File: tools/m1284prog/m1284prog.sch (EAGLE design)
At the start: 10 parts, among them IC1 ATMEGA644-20PU, J1 AVR_SPI_PROG_3X2PTH

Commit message: Update several tool boards.
+ AEPRO had the wrong socket size; the ZIF footprint was for
  a narrow 28-pin DIP.
+ AEPRO was missing an inverter on the LEDs.
+ M328PGM had a serial line tied to RST: any attempt at using the
  UART caused the board to reset.
+ M1284PGM had no silkscreen markings to identify the board.
+ M1284PGM had no decoupling capacitor for the MCU.
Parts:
- added C1: 0.1uF, capacitor-wima:C2,5-3
- R1: value (none) -> 10K
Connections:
- net GND: now also C1.2
- net VCC: now also C1.1
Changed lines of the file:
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@@
 <drawing>
 <settings>
-<setting alwaysvectorfont="yes"/>
+<setting alwaysvectorfont="no"/>
 <setting verticaltext="up"/>
 </settings>
@@
 <part name="SUPPLY1" library="SparkFun-PowerSymbols" deviceset="VCC" device=""/>
 <part name="GND1" library="SparkFun-PowerSymbols" deviceset="GND" device=""/>
-<part name="R1" library="SparkFun-Resistors" deviceset="RESISTOR" device="AXIAL-0.3" value=" "/>
+<part name="R1" library="SparkFun-Resistors" deviceset="RESISTOR" device="AXIAL-0.3" value="10K"/>
 <part name="S1" library="SparkFun-Retired" deviceset="TAC_SWITCH" device="PTH"/>
 <part name="J1" library="SparkFun-Connectors" deviceset="AVR_SPI_PROG_3X2" device="PTH"/>
@@
 <part name="GND5" library="SparkFun-PowerSymbols" deviceset="GND" device=""/>
 <part name="CN1" library="microbuilder" deviceset="FTDIUSBCABLE" device=""/>
+<part name="C1" library="capacitor-wima" library_urn="urn:adsk.eagle:library:116" deviceset="C" device="2,5-3" package3d_urn="urn:adsk.eagle:package:5436/1" value="0.1uF"/>
 </parts>
 <sheets>
@@
 <attribute name="VALUE" x="0" y="-2.54" size="1.27" layer="96" rot="R180"/>
 </instance>
+<instance part="C1" gate="G$1" x="-27.94" y="25.4" smashed="yes">
+<attribute name="NAME" x="-26.416" y="25.781" size="1.778" layer="95"/>
+<attribute name="VALUE" x="-26.416" y="20.701" size="1.778" layer="96"/>
+</instance>
 </instances>
 <busses>
@@
 <wire x1="-5.08" y1="20.32" x2="-22.86" y2="20.32" width="0.1524" layer="91"/>
 <pinref part="GND1" gate="1" pin="GND"/>
-<wire x1="-22.86" y1="20.32" x2="-22.86" y2="7.62" width="0.1524" layer="91"/>
+<wire x1="-22.86" y1="20.32" x2="-22.86" y2="17.78" width="0.1524" layer="91"/>
 <pinref part="S1" gate="S" pin="2"/>
+<wire x1="-22.86" y1="17.78" x2="-22.86" y2="7.62" width="0.1524" layer="91"/>
 <wire x1="-22.86" y1="7.62" x2="-22.86" y2="2.54" width="0.1524" layer="91"/>
 <wire x1="-33.02" y1="27.94" x2="-33.02" y2="7.62" width="0.1524" layer="91"/>
@@
 <wire x1="10.16" y1="22.86" x2="10.16" y2="7.62" width="0.1524" layer="91"/>
 <wire x1="10.16" y1="7.62" x2="-22.86" y2="7.62" width="0.1524" layer="91"/>
+<pinref part="C1" gate="G$1" pin="2"/>
+<wire x1="-27.94" y1="20.32" x2="-27.94" y2="17.78" width="0.1524" layer="91"/>
+<wire x1="-27.94" y1="17.78" x2="-22.86" y2="17.78" width="0.1524" layer="91"/>
+<junction x="-22.86" y="17.78"/>
 </segment>
 <segment>
@@
 <wire x1="25.4" y1="25.4" x2="-22.86" y2="25.4" width="0.1524" layer="91"/>
 <pinref part="SUPPLY1" gate="G$1" pin="VCC"/>
-<wire x1="-22.86" y1="25.4" x2="-22.86" y2="50.8" width="0.1524" layer="91"/>
+<wire x1="-22.86" y1="25.4" x2="-22.86" y2="30.48" width="0.1524" layer="91"/>
 <pinref part="R1" gate="G$1" pin="2"/>
+<wire x1="-22.86" y1="30.48" x2="-22.86" y2="50.8" width="0.1524" layer="91"/>
 <wire x1="-22.86" y1="50.8" x2="-22.86" y2="58.42" width="0.1524" layer="91"/>
 <wire x1="-33.02" y1="50.8" x2="-22.86" y2="50.8" width="0.1524" layer="91"/>
 <junction x="-22.86" y="50.8"/>
-</segment>
-<segment>
+<pinref part="C1" gate="G$1" pin="1"/>
+<wire x1="-27.94" y1="27.94" x2="-27.94" y2="30.48" width="0.1524" layer="91"/>
+<wire x1="-27.94" y1="30.48" x2="-22.86" y2="30.48" width="0.1524" layer="91"/>
+<junction x="-22.86" y="30.48"/>
+</segment>
+<segment>

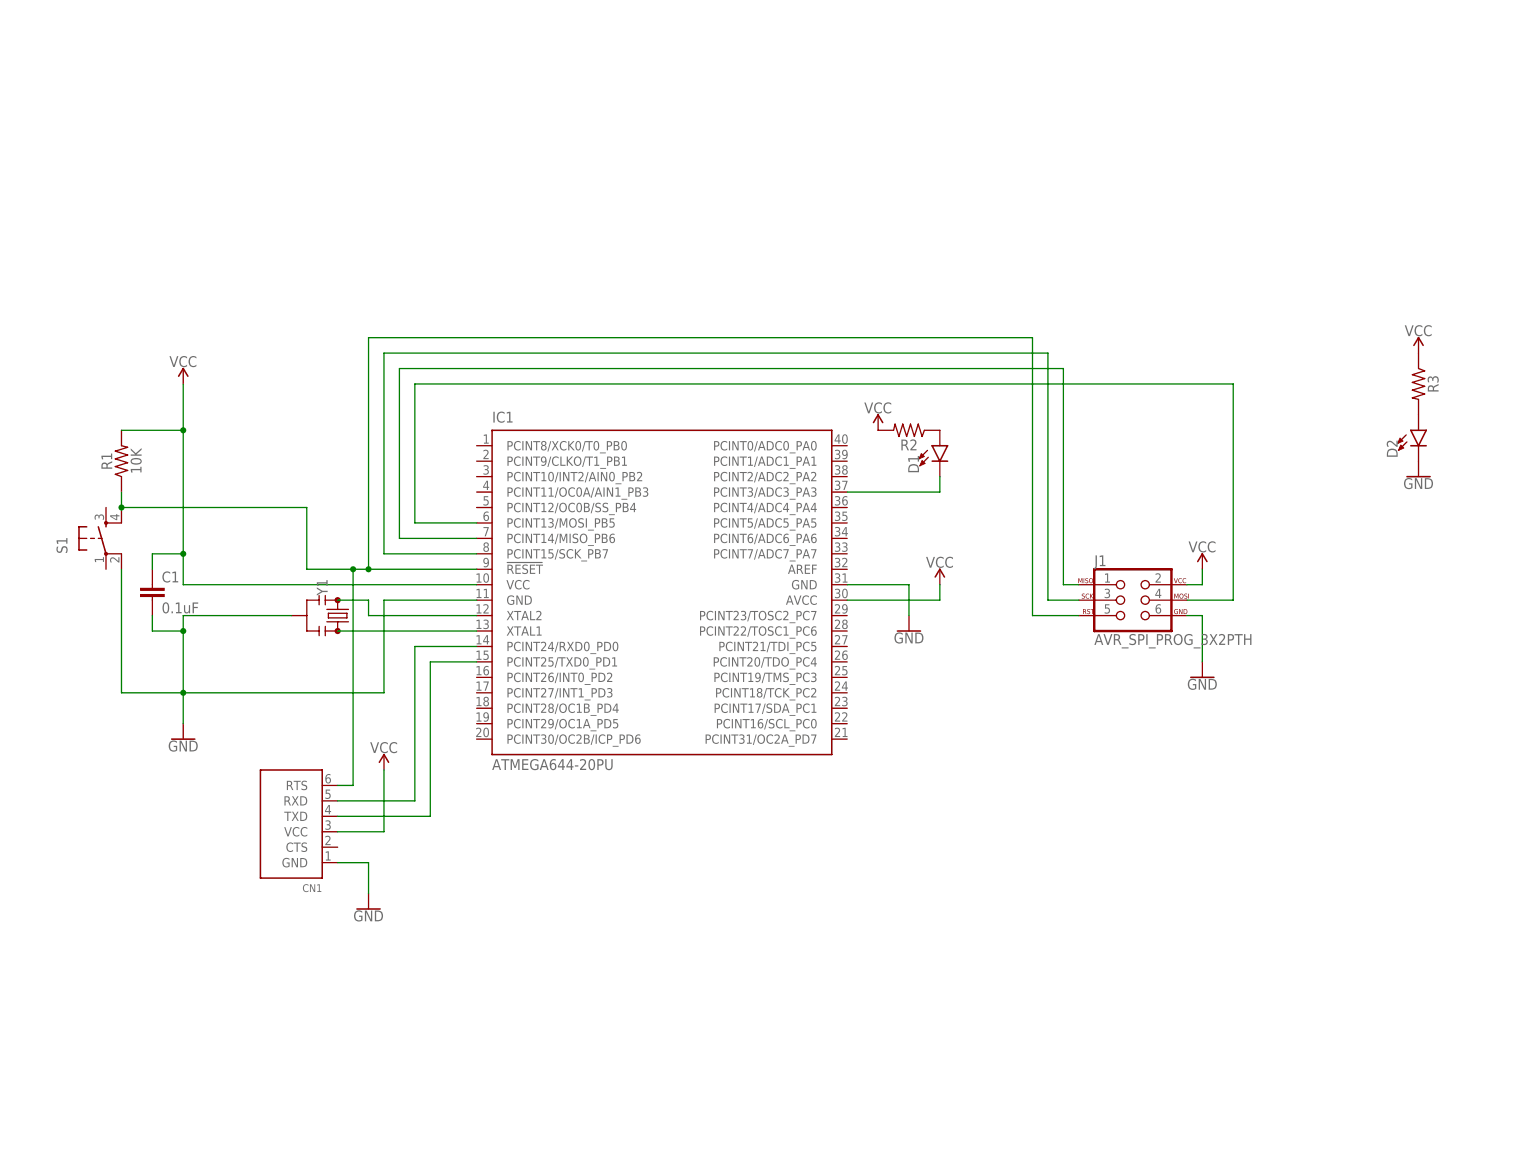
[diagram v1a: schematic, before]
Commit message: Fix UART issues in programmers.
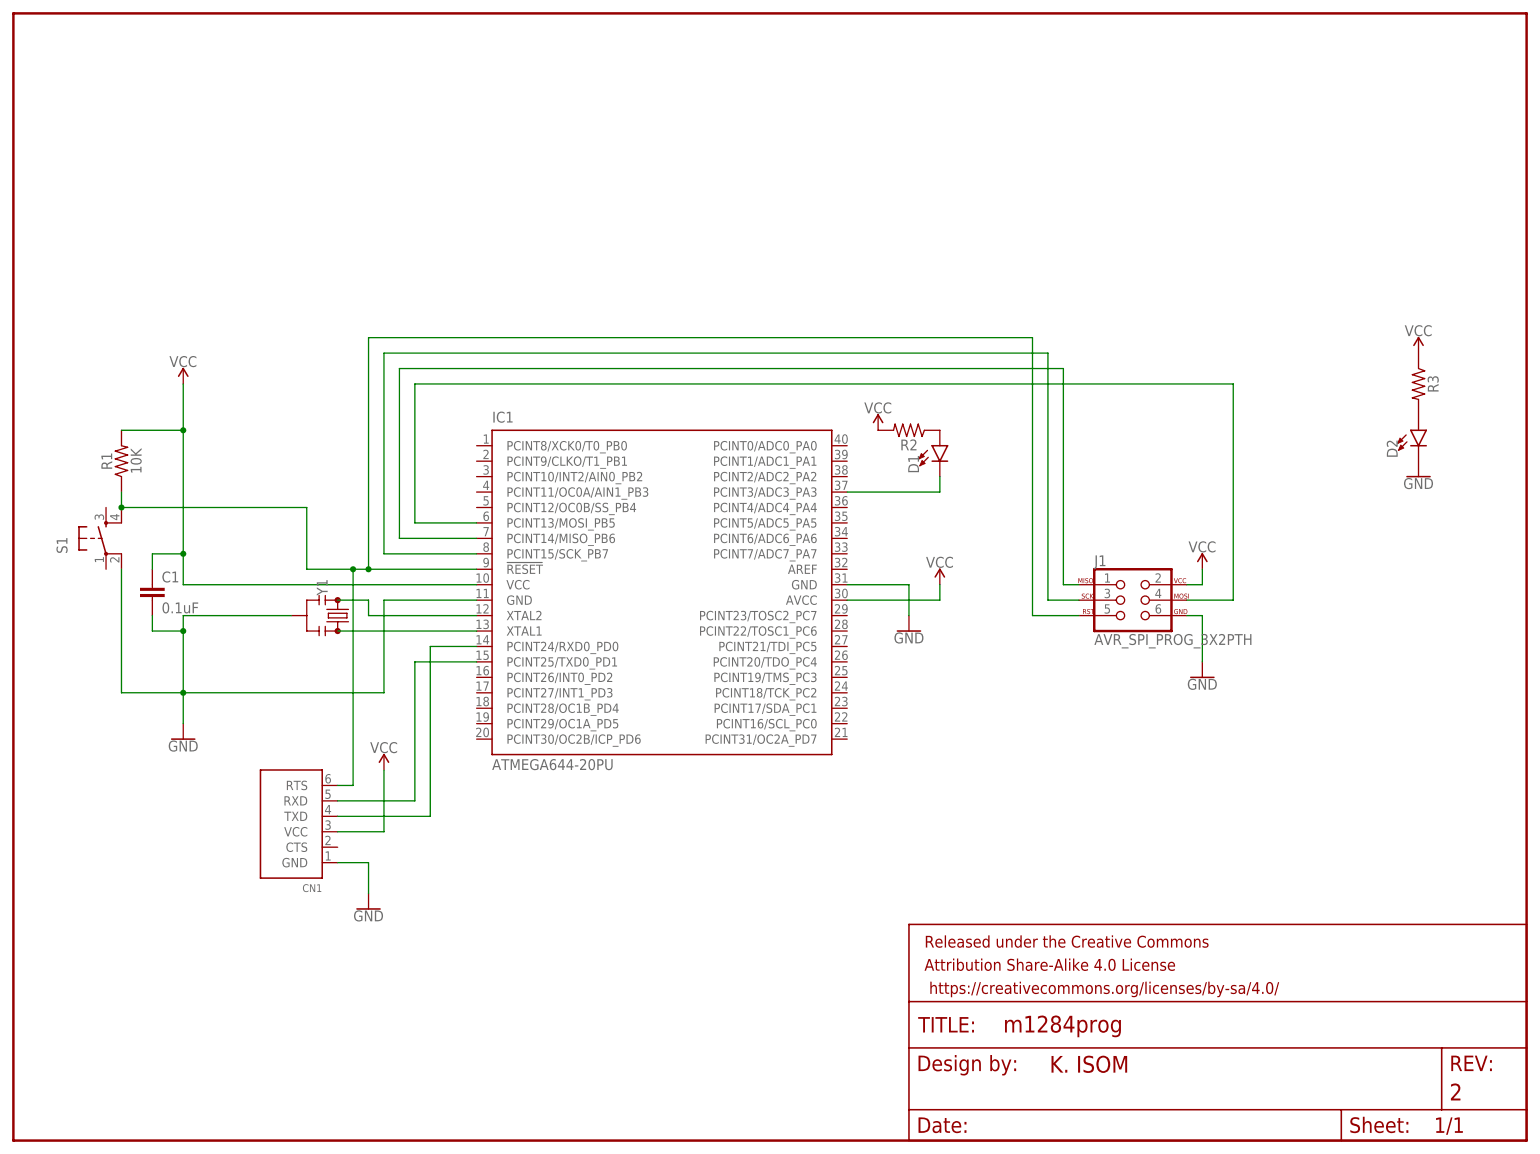
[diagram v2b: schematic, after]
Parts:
- added FRAME1: FRAME-LETTER, SparkFun-Aesthetics:FRAME-LETTER
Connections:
- removed net N$12: CN1.RXD, IC1.PCINT24/RXD0_PD0
- removed net N$13: CN1.TXD, IC1.PCINT25/TXD0_PD1
- new net N$10: CN1.RXD, IC1.PCINT25/TXD0_PD1
- new net N$9: CN1.TXD, IC1.PCINT24/RXD0_PD0
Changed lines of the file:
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@@
 <drawing>
 <settings>
-<setting alwaysvectorfont="no"/>
+<setting alwaysvectorfont="yes"/>
 <setting verticaltext="up"/>
 </settings>
@@
 <layer number="115" name="ReferenceISLANDS" color="7" fill="1" visible="yes" active="yes"/>
 <layer number="116" name="Patch_BOT" color="9" fill="4" visible="yes" active="yes"/>
+<layer number="117" name="PM_Ref" color="26" fill="1" visible="yes" active="yes"/>
 <layer number="118" name="Rect_Pads" color="7" fill="1" visible="yes" active="yes"/>
+<layer number="119" name="PF_Ref" color="31" fill="1" visible="yes" active="yes"/>
+<layer number="120" name="WFL_Ref" color="25" fill="1" visible="yes" active="yes"/>
 <layer number="121" name="_tsilk" color="7" fill="1" visible="yes" active="yes"/>
 <layer number="122" name="_bsilk" color="7" fill="1" visible="yes" active="yes"/>
@@
 <part name="CN1" library="microbuilder" deviceset="FTDIUSBCABLE" device=""/>
 <part name="C1" library="capacitor-wima" library_urn="urn:adsk.eagle:library:116" deviceset="C" device="2,5-3" package3d_urn="urn:adsk.eagle:package:5436/1" value="0.1uF"/>
+<part name="FRAME1" library="SparkFun-Aesthetics" deviceset="FRAME-LETTER" device="">
+<attribute name="DESIGNER" value="K. ISOM"/>
+<attribute name="REV" value="2"/>
+</part>
 </parts>
 <sheets>
@@
 <attribute name="NAME" x="-26.416" y="25.781" size="1.778" layer="95"/>
 <attribute name="VALUE" x="-26.416" y="20.701" size="1.778" layer="96"/>
+</instance>
+<instance part="FRAME1" gate="G$1" x="-50.8" y="-66.04" smashed="yes"/>
+<instance part="FRAME1" gate="V" x="96.52" y="-66.04" smashed="yes">
+<attribute name="LAST_DATE_TIME" x="109.22" y="-64.77" size="2.54" layer="94" font="vector"/>
+<attribute name="SHEET" x="182.88" y="-64.77" size="2.54" layer="94" font="vector"/>
+<attribute name="DRAWING_NAME" x="112.014" y="-48.26" size="2.7432" layer="94" font="vector"/>
+<attribute name="DESIGNER" x="119.634" y="-54.864" size="2.7432" layer="94" font="vector"/>
+<attribute name="REV" x="185.42" y="-59.436" size="2.7432" layer="94" font="vector"/>
 </instance>
 </instances>
@@
 </segment>
 </net>
-<net name="N$12" class="0">
+<net name="N$9" class="0">
+<segment>
+<pinref part="CN1" gate="G$1" pin="TXD"/>
+<wire x1="2.54" y1="-12.7" x2="17.78" y2="-12.7" width="0.1524" layer="91"/>
+<pinref part="IC1" gate="G$1" pin="PCINT24/RXD0_PD0"/>
+<wire x1="17.78" y1="15.24" x2="25.4" y2="15.24" width="0.1524" layer="91"/>
+<wire x1="17.78" y1="-12.7" x2="17.78" y2="15.24" width="0.1524" layer="91"/>
+</segment>
+</net>
+<net name="N$10" class="0">
 <segment>
 <pinref part="CN1" gate="G$1" pin="RXD"/>
 <wire x1="2.54" y1="-10.16" x2="15.24" y2="-10.16" width="0.1524" layer="91"/>
-<wire x1="15.24" y1="-10.16" x2="15.24" y2="15.24" width="0.1524" layer="91"/>
-<pinref part="IC1" gate="G$1" pin="PCINT24/RXD0_PD0"/>
-<wire x1="15.24" y1="15.24" x2="25.4" y2="15.24" width="0.1524" layer="91"/>
-</segment>
-</net>
-<net name="N$13" class="0">
-<segment>
-<pinref part="CN1" gate="G$1" pin="TXD"/>
-<wire x1="2.54" y1="-12.7" x2="17.78" y2="-12.7" width="0.1524" layer="91"/>
-<wire x1="17.78" y1="-12.7" x2="17.78" y2="12.7" width="0.1524" layer="91"/>
 <pinref part="IC1" gate="G$1" pin="PCINT25/TXD0_PD1"/>
-<wire x1="17.78" y1="12.7" x2="25.4" y2="12.7" width="0.1524" layer="91"/>
-</segment>
-</net>
+<wire x1="15.24" y1="12.7" x2="25.4" y2="12.7" width="0.1524" layer="91"/>
+<wire x1="15.24" y1="-10.16" x2="15.24" y2="12.7" width="0.1524" layer="91"/>
+</segment>
+</net>
